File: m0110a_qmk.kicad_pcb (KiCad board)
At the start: 2 copper layers, 380 x 137.9 mm, 179 parts, among them J1 AVR-ISP-6, J2 USB_B_Mini, U1 ATmega32A-PU, Y1 16Mhz

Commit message: cosmetic stuff
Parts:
- added G***: LOGO, custom_parts:qr, B.Cu at (212.1, 162.8)
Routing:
- net col8: track 247.2 -> 242.4 mm
- net col7: track 136.3 -> 132.3 mm

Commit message: change logos
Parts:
- removed the G*** at (106.7, 156.7)
- added G***: LOGO, custom_parts:pear_x_elmo, B.Cu at (109.5, 157.0)
- added G***: LOGO, custom_parts:qmk, B.Cu at (107.7, 176.5)
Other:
- board text added: "M0110a USB PCB v0.1"
- board text removed: "M0110a QMK PCB v0.1"

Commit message: more logos!
now in copper :)
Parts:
- added G***: LOGO, custom_parts:qmk_copper, F.Cu at (105.9, 169.4)
- added G***: LOGO, custom_parts:pear_x_elmo_copper, F.Cu at (104.6, 156.2)

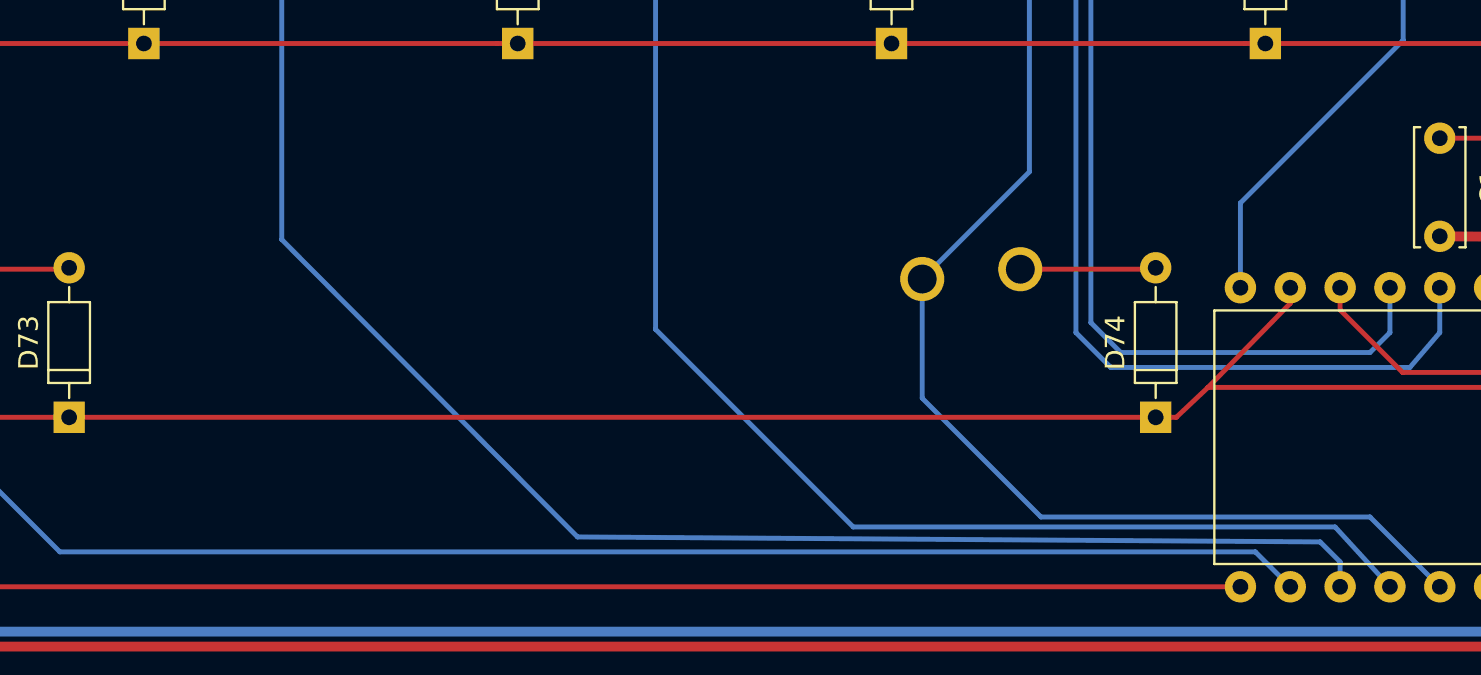
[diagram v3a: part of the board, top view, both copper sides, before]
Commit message: fixed logos
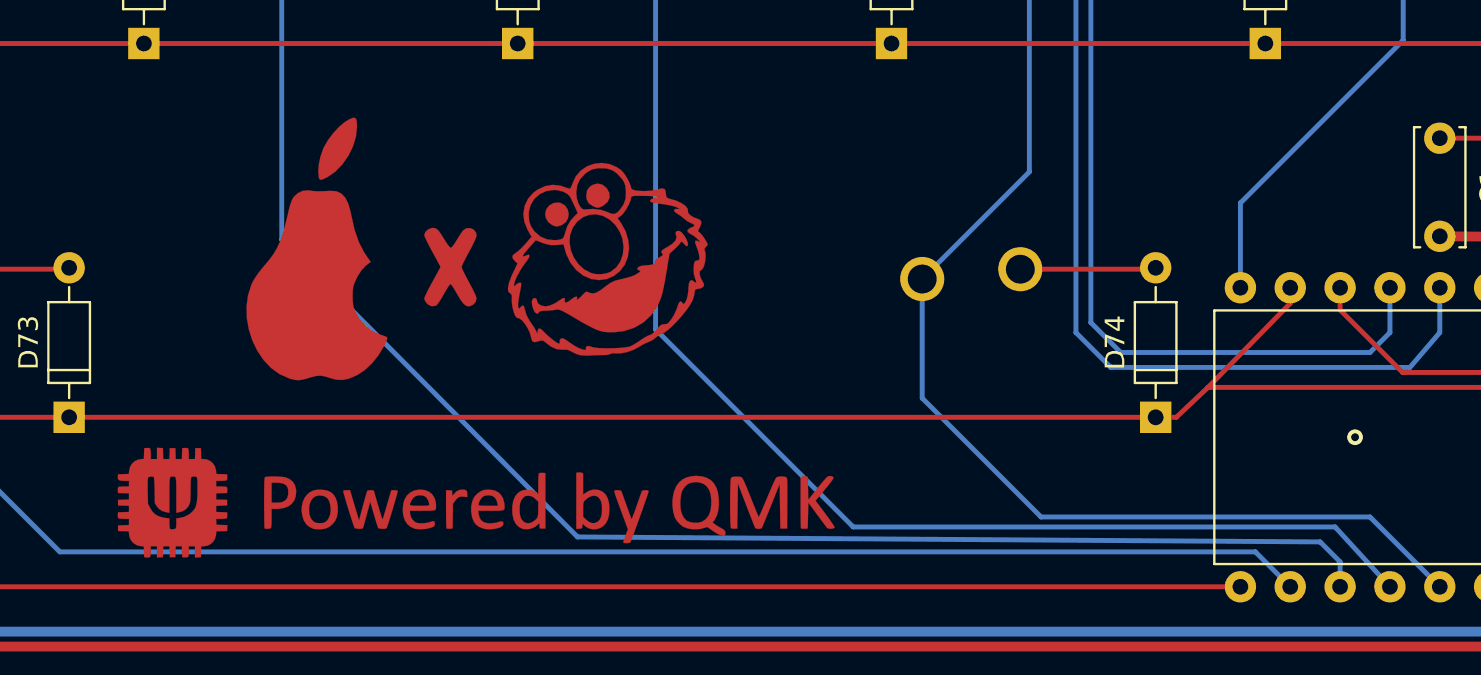
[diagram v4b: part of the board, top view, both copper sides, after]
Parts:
- moved G*** 0.25 mm to (106.2, 169.4)
- moved G*** 0.25 mm to (104.6, 156.5)
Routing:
- net GND: vias 2 -> 3

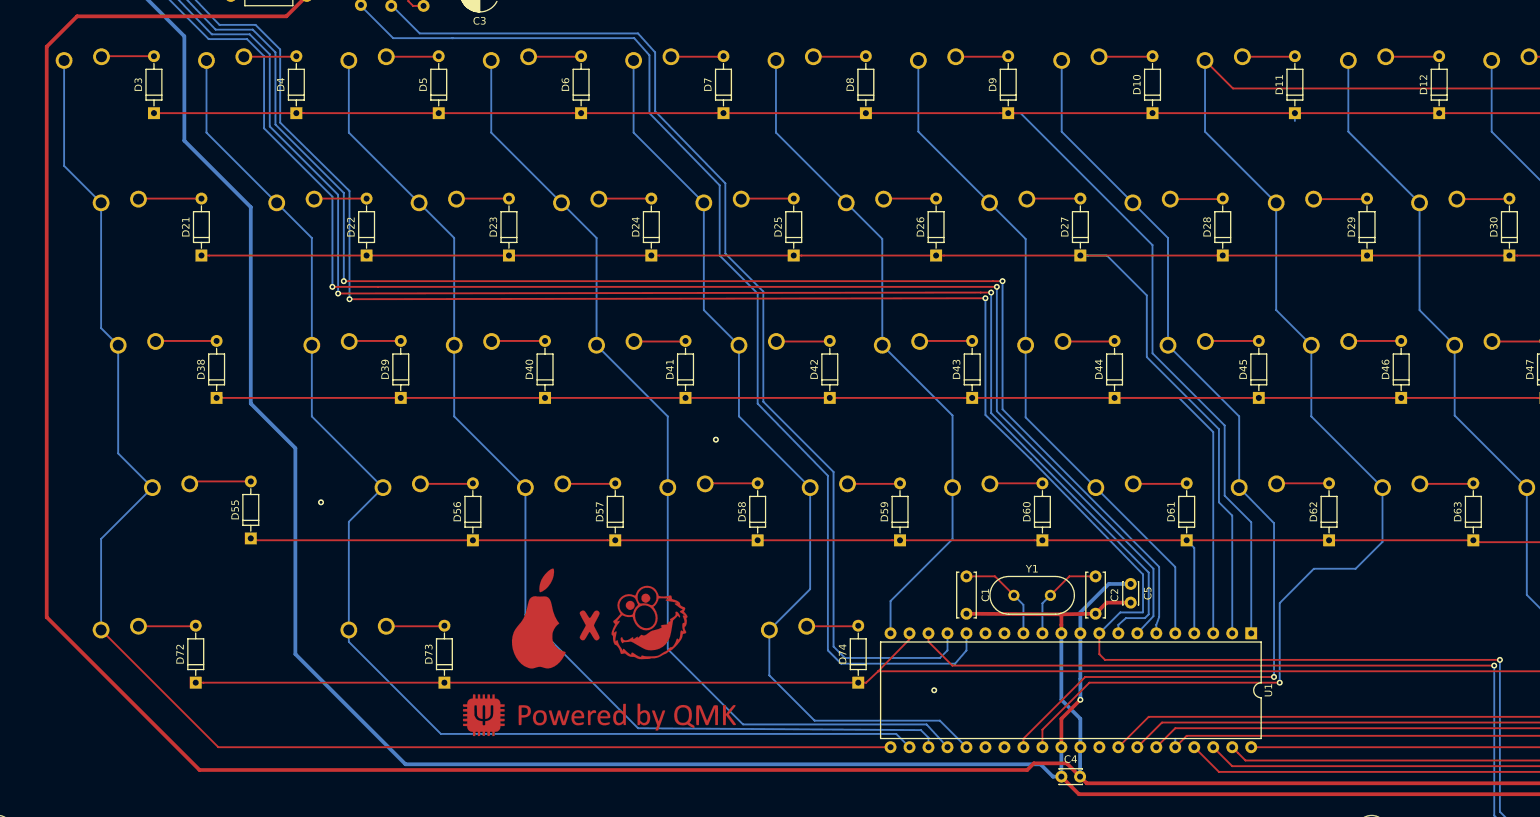
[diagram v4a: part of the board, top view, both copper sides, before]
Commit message: some trace changes
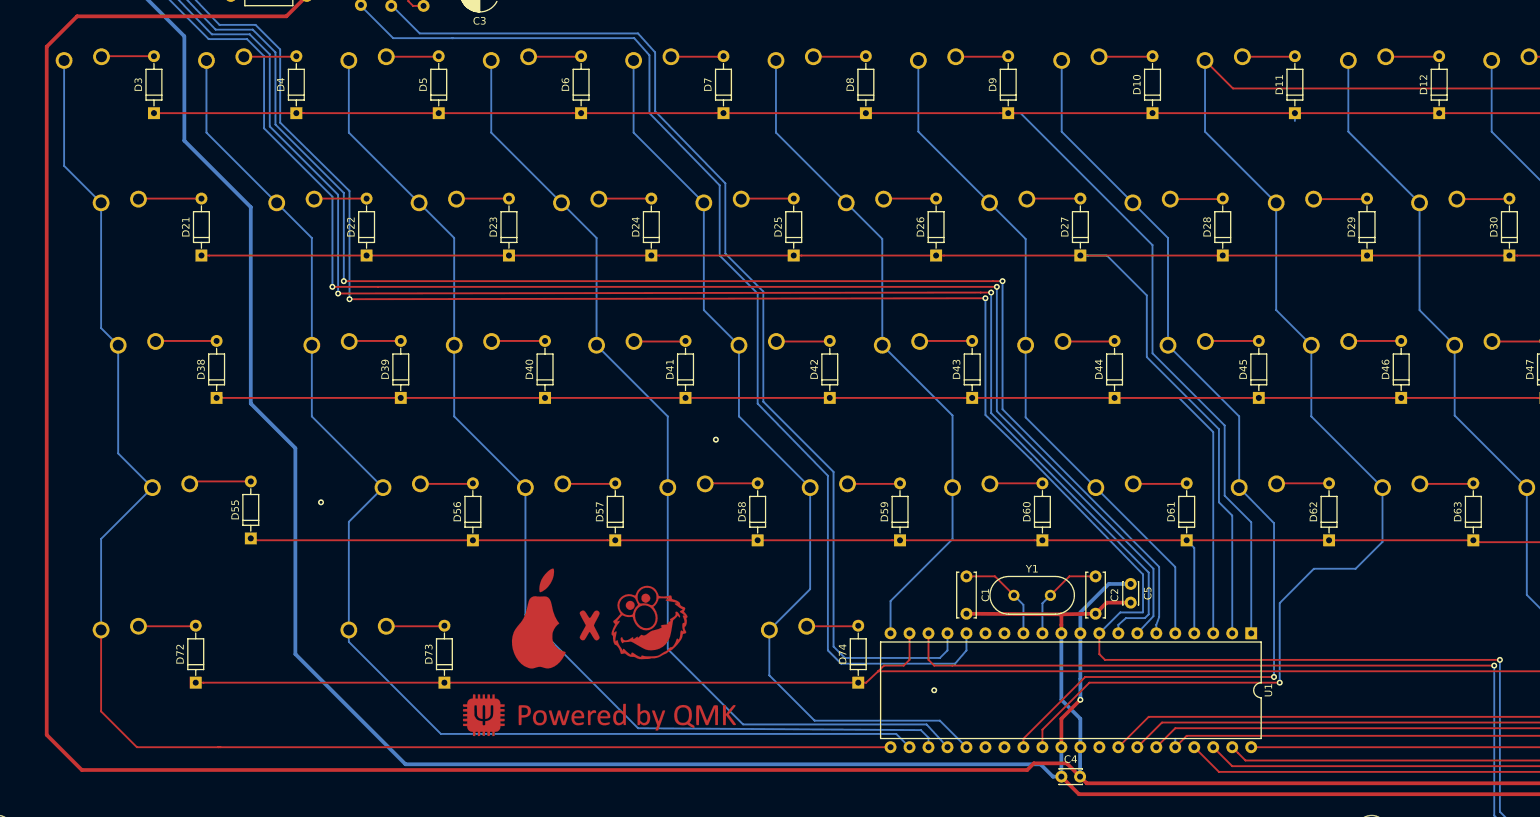
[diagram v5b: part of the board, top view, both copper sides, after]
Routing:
- net GND: track 483.3 -> 492.5 mm
- net col0: track 196.1 -> 202.5 mm
- net row4: track 447.7 -> 450.0 mm
- net boot: track 157.8 -> 159.2 mm
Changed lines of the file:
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@@
     (thickness 1.6)
     (drawings 57)
-    (tracks 763)
+    (tracks 771)
     (zones 0)
     (modules 183)
@@
     (34 B.Paste user)
     (35 F.Paste user)
-    (36 B.SilkS user hide)
+    (36 B.SilkS user)
     (37 F.SilkS user)
     (38 B.Mask user)
@@
   (segment (start 276.496213 183.824) (end 281.582 183.824) (width 0.25) (layer F.Cu) (net 1))
   (segment (start 275.082 183.824) (end 276.496213 183.824) (width 0.25) (layer F.Cu) (net 1))
-  (segment (start 225.806 162.814) (end 153.30063 162.814) (width 0.25) (layer F.Cu) (net 1))
-  (segment (start 150.114 159.62737) (end 150.114 158.496) (width 0.25) (layer F.Cu) (net 1))
   (via (at 225.806 162.814) (size 0.8) (drill 0.4) (layers F.Cu B.Cu) (net 1))
-  (segment (start 153.30063 162.814) (end 150.114 159.62737) (width 0.25) (layer F.Cu) (net 1))
   (segment (start 270.946 187.96) (end 275.082 183.824) (width 0.25) (layer B.Cu) (net 1))
   (segment (start 230.886 187.96) (end 270.946 187.96) (width 0.25) (layer B.Cu) (net 1))
   (segment (start 225.806 162.814) (end 225.806 182.88) (width 0.25) (layer B.Cu) (net 1))
   (segment (start 225.806 182.88) (end 230.886 187.96) (width 0.25) (layer B.Cu) (net 1))
+  (segment (start 153.30063 162.814) (end 225.806 162.814) (width 0.25) (layer F.Cu) (net 1))
+  (segment (start 150.876 162.814) (end 153.30063 162.814) (width 0.25) (layer F.Cu) (net 1))
+  (segment (start 150.114 158.496) (end 150.114 162.052) (width 0.25) (layer F.Cu) (net 1))
+  (segment (start 150.114 162.052) (end 150.876 162.814) (width 0.25) (layer F.Cu) (net 1))
   (segment (start 62.865 61.7855) (end 62.865 65.5955) (width 0.5) (layer B.Cu) (net 2))
   (segment (start 170.394 173.776) (end 170.434 173.736) (width 0.5) (layer B.Cu) (net 2))
@@
   (segment (start 173.95 154.392) (end 172.466 155.876) (width 0.5) (layer F.Cu) (net 2))
   (segment (start 177.165 154.392) (end 173.95 154.392) (width 0.5) (layer F.Cu) (net 2))
-  (segment (start 64.1985 75.946) (end 66.929 73.2155) (width 0.5) (layer F.Cu) (net 2))
-  (segment (start 32.131 80.01) (end 36.195 75.946) (width 0.5) (layer F.Cu) (net 2))
-  (segment (start 32.131 156.337) (end 32.131 80.01) (width 0.5) (layer F.Cu) (net 2))
-  (segment (start 52.578 176.784) (end 32.131 156.337) (width 0.5) (layer F.Cu) (net 2))
-  (segment (start 36.195 75.946) (end 64.1985 75.946) (width 0.5) (layer F.Cu) (net 2))
-  (segment (start 170.394 177.673) (end 168.616 175.895) (width 0.5) (layer F.Cu) (net 2))
-  (segment (start 168.616 175.895) (end 164.211 175.895) (width 0.5) (layer F.Cu) (net 2))
-  (segment (start 164.211 175.895) (end 163.322 176.784) (width 0.5) (layer F.Cu) (net 2))
-  (segment (start 163.322 176.784) (end 52.578 176.784) (width 0.5) (layer F.Cu) (net 2))
   (segment (start 82.474 61.029) (end 82.474 61.9) (width 0.5) (layer B.Cu) (net 2))
   (segment (start 82.474 61.9) (end 84.963 64.389) (width 0.5) (layer B.Cu) (net 2))
@@
   (via (at 121.666 132.588) (size 0.8) (drill 0.4) (layers F.Cu B.Cu) (net 2))
   (via (at 150.876 166.116) (size 0.8) (drill 0.4) (layers F.Cu B.Cu) (net 2))
+  (segment (start 64.1985 75.946) (end 66.929 73.2155) (width 0.5) (layer F.Cu) (net 2))
+  (segment (start 36.195 75.946) (end 64.1985 75.946) (width 0.5) (layer F.Cu) (net 2))
+  (segment (start 168.616 175.895) (end 164.211 175.895) (width 0.5) (layer F.Cu) (net 2))
+  (segment (start 170.394 177.673) (end 168.616 175.895) (width 0.5) (layer F.Cu) (net 2))
+  (segment (start 32.131 172.085) (end 32.131 80.01) (width 0.5) (layer F.Cu) (net 2))
+  (segment (start 164.211 175.895) (end 163.322 176.784) (width 0.5) (layer F.Cu) (net 2))
+  (segment (start 163.322 176.784) (end 36.83 176.784) (width 0.5) (layer F.Cu) (net 2))
+  (segment (start 32.131 80.01) (end 36.195 75.946) (width 0.5) (layer F.Cu) (net 2))
+  (segment (start 36.83 176.784) (end 32.131 172.085) (width 0.5) (layer F.Cu) (net 2))
   (segment (start 159.004 150.876) (end 161.544 153.416) (width 0.25) (layer F.Cu) (net 3))
   (segment (start 155.194 150.876) (end 159.004 150.876) (width 0.25) (layer F.Cu) (net 3))
@@
   (segment (start 246.888 165.1) (end 245.838 165.1) (width 0.25) (layer F.Cu) (net 80))
   (segment (start 141.766 165.1) (end 143.383 163.576) (width 0.25) (layer F.Cu) (net 80))
-  (segment (start 143.383 163.576) (end 147.574 159.292) (width 0.25) (layer F.Cu) (net 80))
   (segment (start 306.104 165.1) (end 305.054 165.1) (width 0.25) (layer B.Cu) (net 80))
   (segment (start 310.896 160.308) (end 306.104 165.1) (width 0.25) (layer B.Cu) (net 80))
+  (segment (start 147.574 158.496) (end 147.574 162.052) (width 0.25) (layer F.Cu) (net 80))
+  (segment (start 147.574 162.052) (end 146.812 162.814) (width 0.25) (layer F.Cu) (net 80))
+  (segment (start 144.145 162.814) (end 143.383 163.576) (width 0.25) (layer F.Cu) (net 80))
+  (segment (start 146.812 162.814) (end 144.145 162.814) (width 0.25) (layer F.Cu) (net 80))
   (segment (start 51.998 157.552) (end 52.07 157.48) (width 0.25) (layer F.Cu) (net 81))
   (segment (start 44.41 157.552) (end 51.998 157.552) (width 0.25) (layer F.Cu) (net 81))
@@
   (segment (start 39.41 145.86) (end 39.41 158.052) (width 0.25) (layer B.Cu) (net 94))
   (segment (start 46.268 139.002) (end 39.41 145.86) (width 0.25) (layer B.Cu) (net 94))
-  (segment (start 55.094 173.736) (end 39.41 158.052) (width 0.25) (layer F.Cu) (net 94))
-  (segment (start 145.034 173.736) (end 55.094 173.736) (width 0.25) (layer F.Cu) (net 94))
+  (segment (start 145.034 173.736) (end 55.372 173.736) (width 0.25) (layer F.Cu) (net 94))
+  (segment (start 39.41 158.052) (end 39.41 168.95) (width 0.25) (layer F.Cu) (net 94))
+  (segment (start 44.196 173.736) (end 55.118 173.736) (width 0.25) (layer F.Cu) (net 94))
+  (segment (start 55.372 173.736) (end 55.118 173.736) (width 0.25) (layer F.Cu) (net 94))
+  (segment (start 39.41 168.95) (end 44.196 173.736) (width 0.25) (layer F.Cu) (net 94))
+  (segment (start 55.118 173.736) (end 55.094 173.736) (width 0.25) (layer F.Cu) (net 94))
   (segment (start 72.557 143.574) (end 77.129 139.002) (width 0.25) (layer B.Cu) (net 95))
   (segment (start 72.557 158.052) (end 72.557 143.574) (width 0.25) (layer B.Cu) (net 95))

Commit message: fixes for newer keycad versions
fixed pathes for 3d parts
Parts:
- Boot1, Reset1: footprint Buttons_Switches_THT:SW_PUSH_6mm -> Button_Switch_THT:SW_PUSH_6mm
- C1, C2: footprint Capacitors_THT:C_Disc_D6.0mm_W2.5mm_P5.00mm -> Capacitor_THT:C_Disc_D6.0mm_W2.5mm_P5.00mm
- C3: footprint Capacitors_THT:CP_Radial_D5.0mm_P2.50mm -> Capacitor_THT:CP_Radial_D5.0mm_P2.50mm
- C4, C5: footprint Capacitors_THT:C_Disc_D3.0mm_W2.0mm_P2.50mm -> Capacitor_THT:C_Disc_D3.0mm_W2.0mm_P2.50mm
- D1, D10, D11, D12, D13, D14, D15, D16, D17, D18, D19, D2, D20, D21, D22, D23, D24, D25, D26, D27, D28, D29, D3, D30, D31, D32, D33, D34, D35, D36, D37, D38, D39, D4, D40, D41, D42, D43, D44, D45, D46, D47, D48, D49, D5, D50, D51, D52, D53, D54, D55, D56, D57, D58, D59, D6, D60, D61, D62, D63, D64, D65, D66, D67, D69, D7, D70, D71, D72, D73, D74, D75, D76, D77, D78, D79, D8, D80, D81, D9: footprint Diodes_THT:D_DO-35_SOD27_P7.62mm_Horizontal -> Diode_THT:D_DO-35_SOD27_P7.62mm_Horizontal
- D82: footprint LEDs:LED_D3.0mm -> LED_THT:LED_D3.0mm
- F1: footprint Fuse_Holders_and_Fuses:Fuse_TE5_Littlefuse-395Series -> Fuse:Fuse_Littelfuse_395Series
- J1: footprint Pin_Headers:Pin_Header_Angled_2x03_Pitch2.54mm -> Connector_PinHeader_2.54mm:PinHeader_2x03_P2.54mm_Horizontal
- R1, R2, R3, R4, R5: footprint Resistors_THT:R_Axial_DIN0207_L6.3mm_D2.5mm_P10.16mm_Horizontal -> Resistor_THT:R_Axial_DIN0207_L6.3mm_D2.5mm_P10.16mm_Horizontal
- U1: footprint Housings_DIP:DIP-40_W15.24mm -> Package_DIP:DIP-40_W15.24mm_Socket
- Y1: footprint Crystals:Crystal_HC49-U_Vertical -> Crystal:Crystal_HC49-4H_Vertical
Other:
- outline, holes or cut-outs redrawn

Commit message: fix some mistakes
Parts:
- removed the G*** at (106.2, 169.4)
- removed the G*** at (104.6, 156.5)
- F1: footprint Fuse:Fuse_Littelfuse_395Series -> custom_parts:Fuse_Littelfuse_395Series
- moved J1 224.3 mm to (239.6, 179.3), turned to 270 degrees
- moved G*** 2.09 mm to (211.6, 164.8)
- moved R1 1.68 mm to (248.2, 183.8)
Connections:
- MX15 pad 1: col14 -> col13
- MX16 pad 1: col15 -> col14
- MX17 pad 1: col16 -> col15
- MX18 pad 1: col17 -> col16
- MX32 pad 1: col14 -> col13
- MX33 pad 1: col15 -> col14
- MX34 pad 1: col16 -> col15
- MX35 pad 1: col17 -> col16
- MX49 pad 1: col14 -> col13
- MX50 pad 1: col15 -> col14
- MX51 pad 1: col16 -> col15
- MX52 pad 1: col17 -> col16
- MX67 pad 1: col14 -> col13
- MX68 pad 1: col15 -> col14
- MX69 pad 1: col16 -> col15
- MX77 pad 1: col14 -> col13
- MX78 pad 1: col16 -> col15
- MX79 pad 1: col17 -> col16
- R5 pad 2: Net-(D1-Pad1) -> Net-(D2-Pad1)
- U1 pad 37: col17 -> col13
- U1 pad 38: col16 -> col14
- U1 pad 40: col14 -> col16
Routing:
- net GND: track 492.5 -> 114.1 mm, vias 3 -> 9
- net col17: track 294.8 -> 0.00 mm, vias 1 -> 0
- net col13: track 0.00 -> 239.0 mm, vias 0 -> 1
- net reset: track 323.5 -> 157.3 mm, vias 3 -> 1
- net MOSI: track 202.6 -> 68.6 mm, vias 2 -> 0
- net SCK: track 202.3 -> 71.0 mm, vias 2 -> 1
- net MISO: track 202.2 -> 71.0 mm, vias 2 -> 1
- net +5V: track 393.0 -> 378.5 mm
- net col15: track 245.1 -> 259.3 mm
- net Net-(D2-Pad1): track 19.3 -> 33.1 mm
- net col16: track 267.5 -> 280.4 mm
- net Net-(D1-Pad1): track 31.7 -> 19.9 mm
- net boot: track 159.2 -> 148.4 mm
- net col14: track 235.6 -> 242.4 mm
- net row4: track 450.0 -> 446.7 mm
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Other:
- board text added: "M0110a USB PCB v0.2"
- board text removed: "M0110a USB PCB v0.1"

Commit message: rev1
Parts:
- removed the C1 at (155.2, 150.9)
- removed the C2 at (172.5, 150.9)
- removed the J2 at (84.1, 54.2)
- added J1: USB_B_Mini, random-keyboard-parts:Molex-0548190519, B.Cu at (84.1, 54.2)
- Boot1: value Boot -> Boot1
- Reset1: value Reset -> Reset1
- Y1: value 16Mhz -> Resonator; footprint Crystal:Crystal_HC49-4H_Vertical -> Crystal:Resonator-3Pin_W7.0mm_H2.5mm
- moved C3 7.24 mm to (170.4, 154.6), turned to 0 degrees
- moved Y1 1.02 mm to (161.5, 154.4)
- moved R3 0.18 mm to (74.3, 64.4)
- renumbered C3 to C1, C4 to C2, C5 to C3, D17 to D16, D18 to D17, D19 to D18, D20 to D19, D21 to D20, D22 to D21, D23 to D22, D24 to D23, D25 to D24, D26 to D25, D27 to D26, D28 to D27, D29 to D28, D30 to D29, D31 to D30, D32 to D31, D33 to D32, D34 to D33, D35 to D34, D36 to D35, D37 to D36, D38 to D37, D39 to D38, D40 to D39, D41 to D40, D42 to D41, D43 to D42, D44 to D43, D45 to D44, D46 to D45, D47 to D46, D48 to D47, D49 to D48, D50 to D49, D51 to D50, D52 to D51, D53 to D52, D54 to D53, D55 to D54, D56 to D55, D57 to D56, D58 to D57, D59 to D58, D60 to D59, D61 to D60, D62 to D61, D63 to D62, D64 to D63, D65 to D64, D66 to D65, D67 to D66, D69 to D67, D70 to D68, D71 to D69, D72 to D70, D73 to D71, D74 to D72, D16 to D73, D75 to D74, D76 to D75, D77 to D76, D78 to D77, D79 to D78, D80 to D79, D81 to D80, J1 to J2, D82 to LED1, MX15 to MX14, MX16 to MX15, MX17 to MX16, MX18 to MX17, MX19 to MX18, MX20 to MX19, MX21 to MX20, MX22 to MX21, MX23 to MX22, MX24 to MX23, MX25 to MX24, MX26 to MX25, MX27 to MX26, MX28 to MX27, MX29 to MX28, MX30 to MX29, MX31 to MX30, MX32 to MX31, MX33 to MX32, MX34 to MX33, MX35 to MX34, MX36 to MX35, MX37 to MX36, MX38 to MX37, MX39 to MX38, MX40 to MX39, MX41 to MX40, MX42 to MX41, MX43 to MX42, MX44 to MX43, MX45 to MX44, MX46 to MX45, MX47 to MX46, MX48 to MX47, MX49 to MX48, MX50 to MX49, MX51 to MX50, MX52 to MX51, MX53 to MX52, MX54 to MX53, MX55 to MX54, MX56 to MX55, MX57 to MX56, MX58 to MX57, MX59 to MX58, MX60 to MX59, MX61 to MX60, MX62 to MX61, MX63 to MX62, MX64 to MX63, MX65 to MX64, MX67 to MX65, MX68 to MX66, MX69 to MX67, MX70 to MX68, MX71 to MX69, MX72 to MX70, MX14 to MX71, MX73 to MX72, MX74 to MX73, MX75 to MX74, MX76 to MX75, MX77 to MX76, MX78 to MX77, MX79 to MX78, R5 to R4, R4 to R5
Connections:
- U1 pad 12: Net-(C2-Pad1) -> Net-(U1-Pad12)
- U1 pad 15: Net-(U1-Pad15) -> col5
- U1 pad 16: D- -> D+
- U1 pad 17: D+ -> D-
- U1 pad 20: col5 -> Net-(U1-Pad20)
- Y1 pad 2: Net-(C2-Pad1) -> GND
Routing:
- net reset: track 157.3 -> 123.8 mm
- net GND: track 114.1 -> 89.0 mm, vias 9 -> 1
- net Net-(C2-Pad1): track 12.6 -> 0.00 mm
- net D-: track 153.3 -> 144.5 mm
- net Net-(U1-Pad13): track 13.0 -> 4.59 mm
- net +5V: track 378.5 -> 371.3 mm
- net Net-(U1-Pad12): track 0.00 -> 4.56 mm
- net MOSI: track 68.6 -> 72.0 mm
- net row0: track 434.0 -> 436.1 mm
- net Net-(D1-Pad1): track 19.9 -> 18.0 mm
- net col5: track 89.9 -> 88.3 mm
- net D+: track 145.7 -> 144.5 mm
- net MISO: track 71.0 -> 72.0 mm
- net SCK: track 71.0 -> 72.0 mm
- net Net-(J2-Pad4): track 0.84 -> 0.00 mm
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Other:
- board text added: "M0110a USB PCB rev1"
- board text added: "nice"
- board text removed: "M0110a USB PCB v0.2"
